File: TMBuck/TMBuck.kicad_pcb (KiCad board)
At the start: 2 copper layers, 13 x 42.5 mm, 6 parts, among them J1 Pins, U1 LM2576S-5

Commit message: Inc Buck
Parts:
- moved C1 1.52 mm to (116.8, 90.7), turned to 270 degrees
- moved L1 0.51 mm to (124.7, 90.6)
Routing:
- net GND: track 1.57 -> 0.00 mm, vias 27 -> 26
- net Net-(D1-Pad1): track 34.1 -> 35.5 mm
- net +5V: track 26.3 -> 25.7 mm

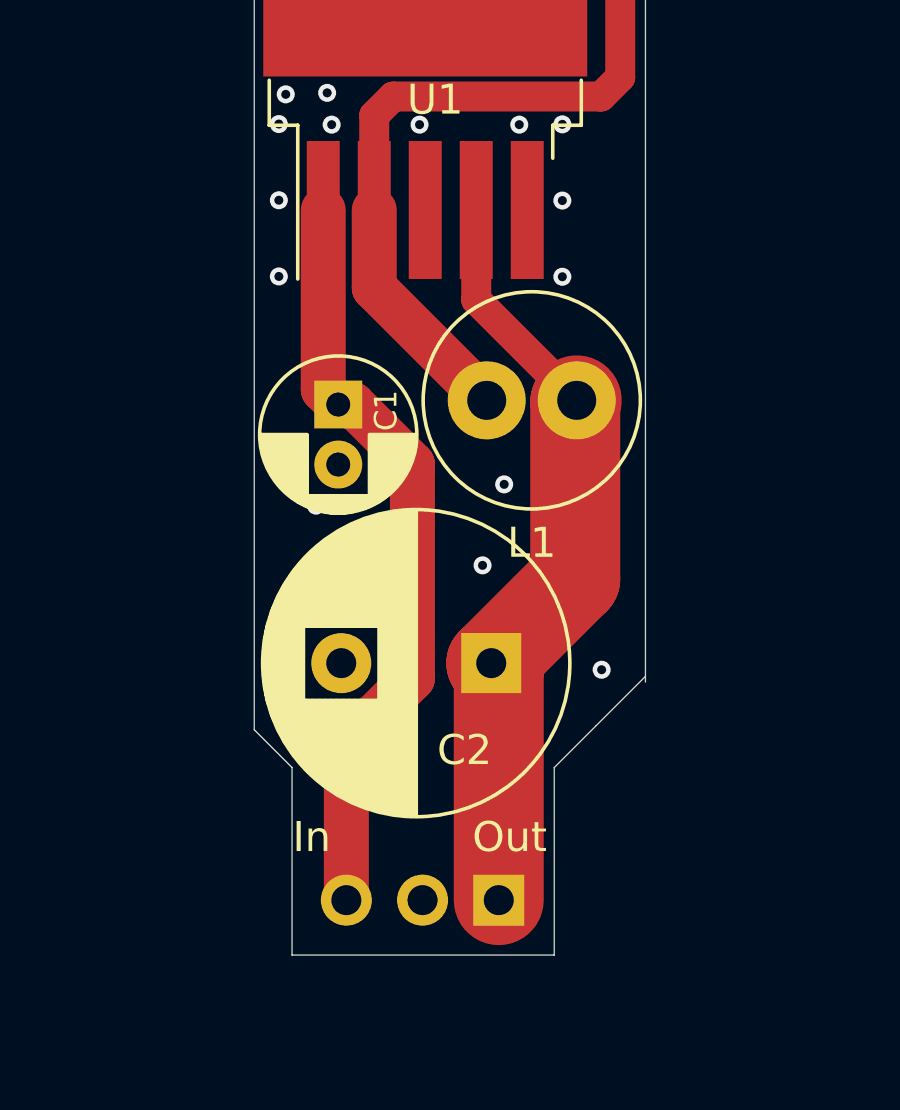
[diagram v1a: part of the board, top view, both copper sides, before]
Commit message: Revert "Inc Buck"
This reverts commit dbd6f2490a180fa10e79e66cec7a5f8d0fb3866e.
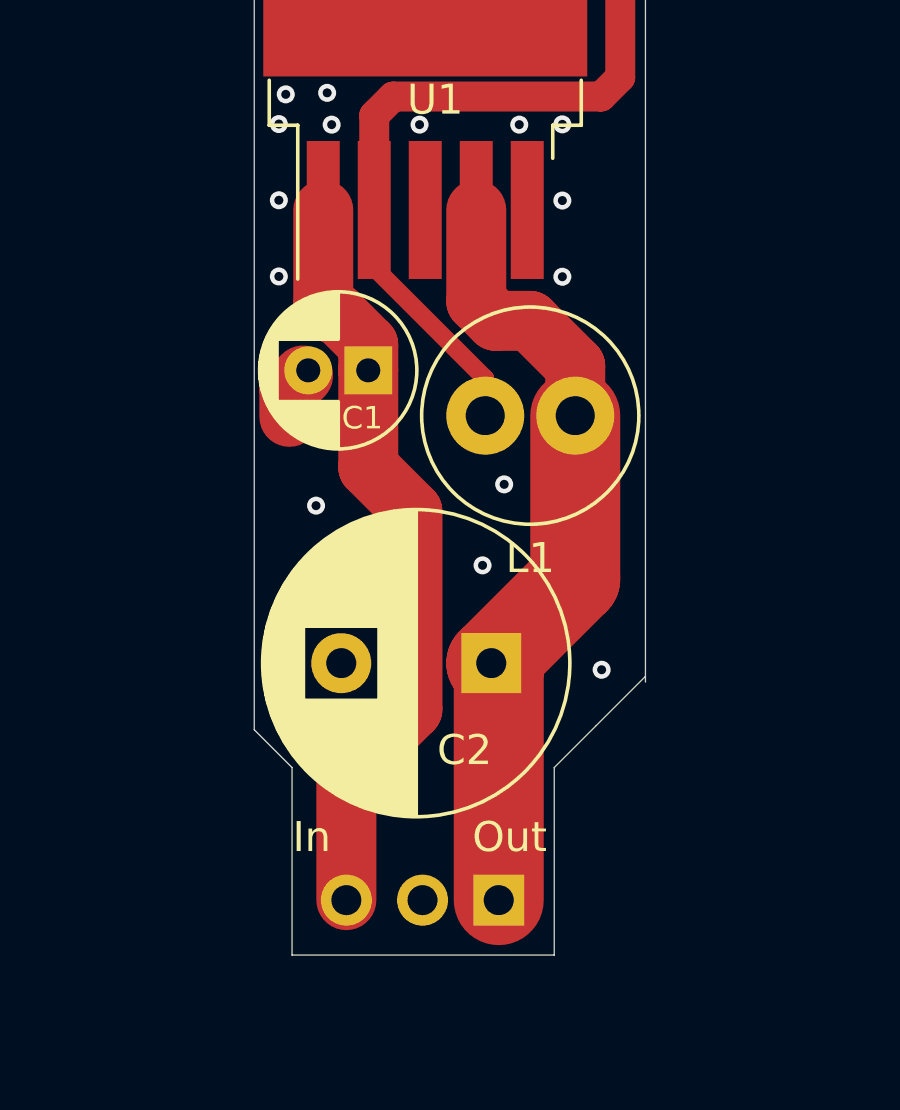
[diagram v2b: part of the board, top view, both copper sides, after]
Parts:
- moved C1 1.52 mm to (117.8, 89.6), turned to 180 degrees
- moved L1 0.51 mm to (124.7, 91.1)
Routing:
- net GND: track 0.00 -> 1.57 mm, vias 26 -> 27
- net Net-(D1-Pad1): track 35.5 -> 34.1 mm
- net +5V: track 25.7 -> 26.3 mm
